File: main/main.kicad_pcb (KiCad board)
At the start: 2 copper layers, 17.8 x 43.2 mm, 6 parts, among them P1 Digital, P2 Analog, P3 CONN_01X01, P4 CONN_01X01, P5 CONN_01X01, P6 CONN_01X01

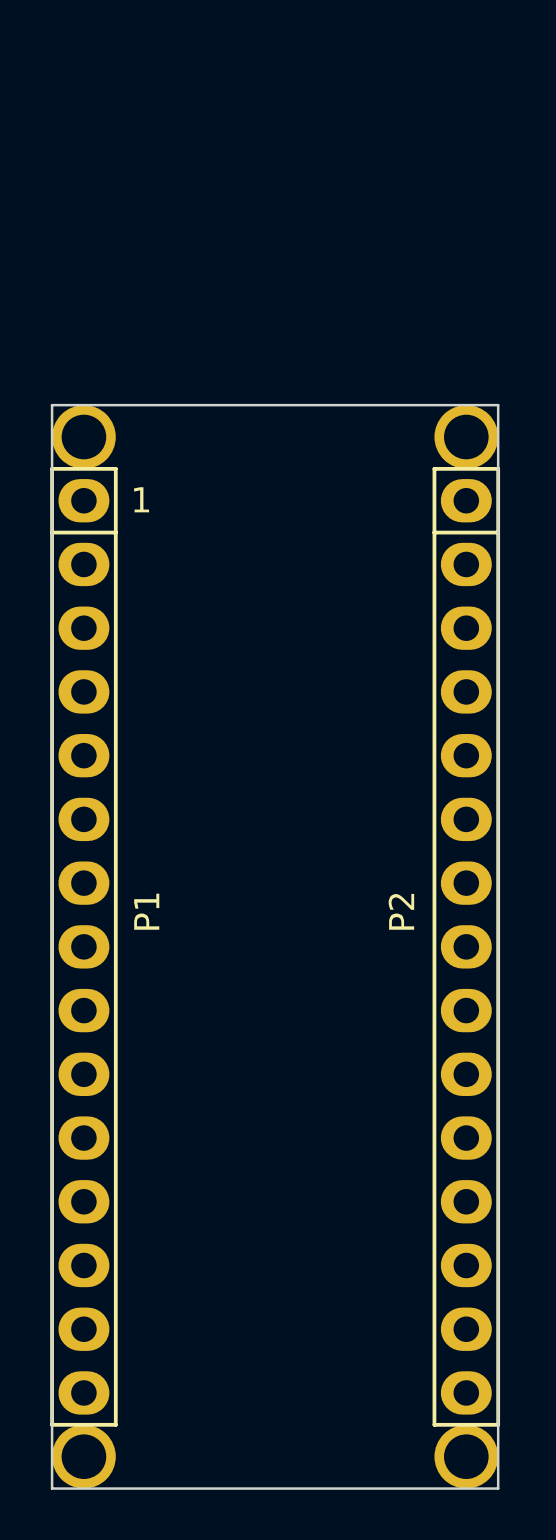
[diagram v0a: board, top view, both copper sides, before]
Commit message: main.pcb: Enlarged outline of board and translated mounting holes
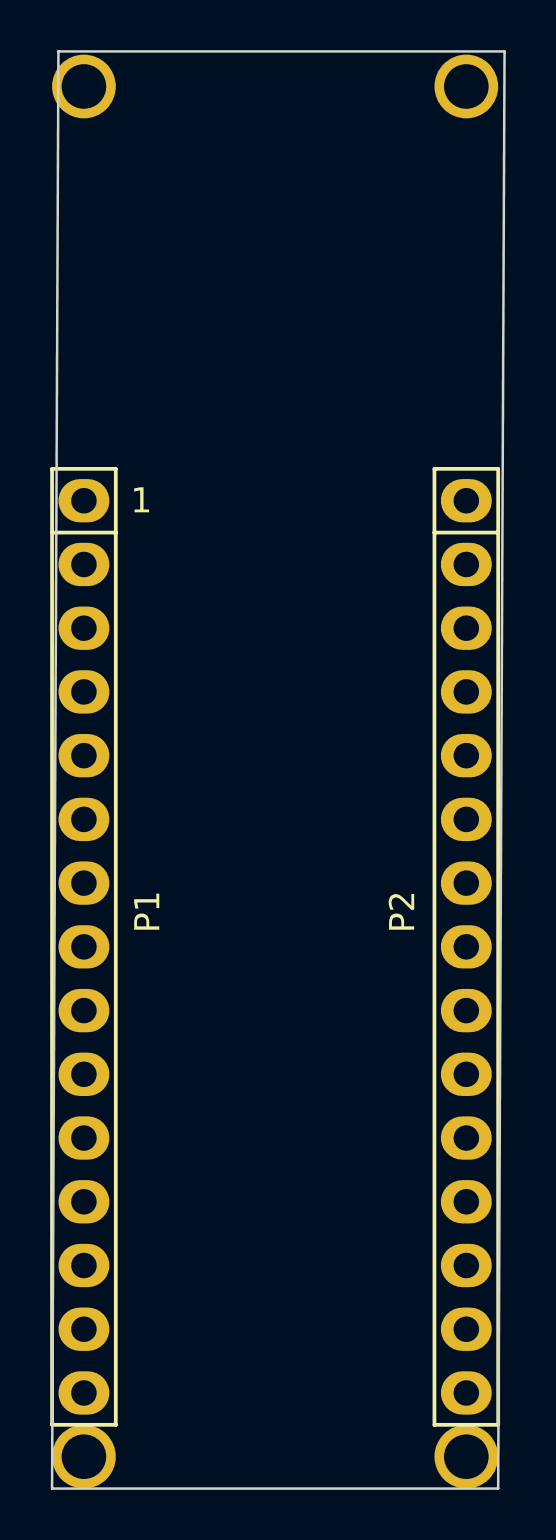
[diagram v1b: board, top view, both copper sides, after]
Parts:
- moved P3 14.0 mm to (139.4, 54.7)
- moved P6 14.0 mm to (154.7, 54.7)
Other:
- board size 17.8 x 43.2 mm -> 18 x 57.3 mm
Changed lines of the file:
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@@
   )
   (module Socket_Arduino_Nano:1pin_Nano locked (layer F.Cu)
-    (at 139.446 68.707)
+    (at 139.446 54.737)
     (descr "module 1 pin (ou trou mecanique de percage)")
     (tags DEV)
@@
   )
   (module Socket_Arduino_Nano:1pin_Nano locked (layer F.Cu)
-    (at 154.686 68.707)
+    (at 154.686 54.737)
     (descr "module 1 pin (ou trou mecanique de percage)")
     (tags DEV)
@@
   (gr_line (start 143.256 72.517) (end 150.876 72.517) (angle 90) (layer Dwgs.User) (width 0.15))
   (gr_line (start 143.256 67.437) (end 143.256 72.517) (angle 90) (layer Dwgs.User) (width 0.15))
-  (gr_line (start 138.176 67.437) (end 138.176 110.617) (angle 90) (layer Edge.Cuts) (width 0.1))
-  (gr_line (start 155.956 67.437) (end 138.176 67.437) (angle 90) (layer Edge.Cuts) (width 0.1))
-  (gr_line (start 155.956 110.617) (end 155.956 67.437) (angle 90) (layer Edge.Cuts) (width 0.1))
+  (gr_line (start 138.43 53.34) (end 138.176 110.617) (angle 90) (layer Edge.Cuts) (width 0.1))
+  (gr_line (start 156.21 53.34) (end 138.43 53.34) (angle 90) (layer Edge.Cuts) (width 0.1))
+  (gr_line (start 155.956 110.617) (end 156.21 53.34) (angle 90) (layer Edge.Cuts) (width 0.1))
   (gr_line (start 138.176 110.617) (end 155.956 110.617) (angle 90) (layer Edge.Cuts) (width 0.1))
 )

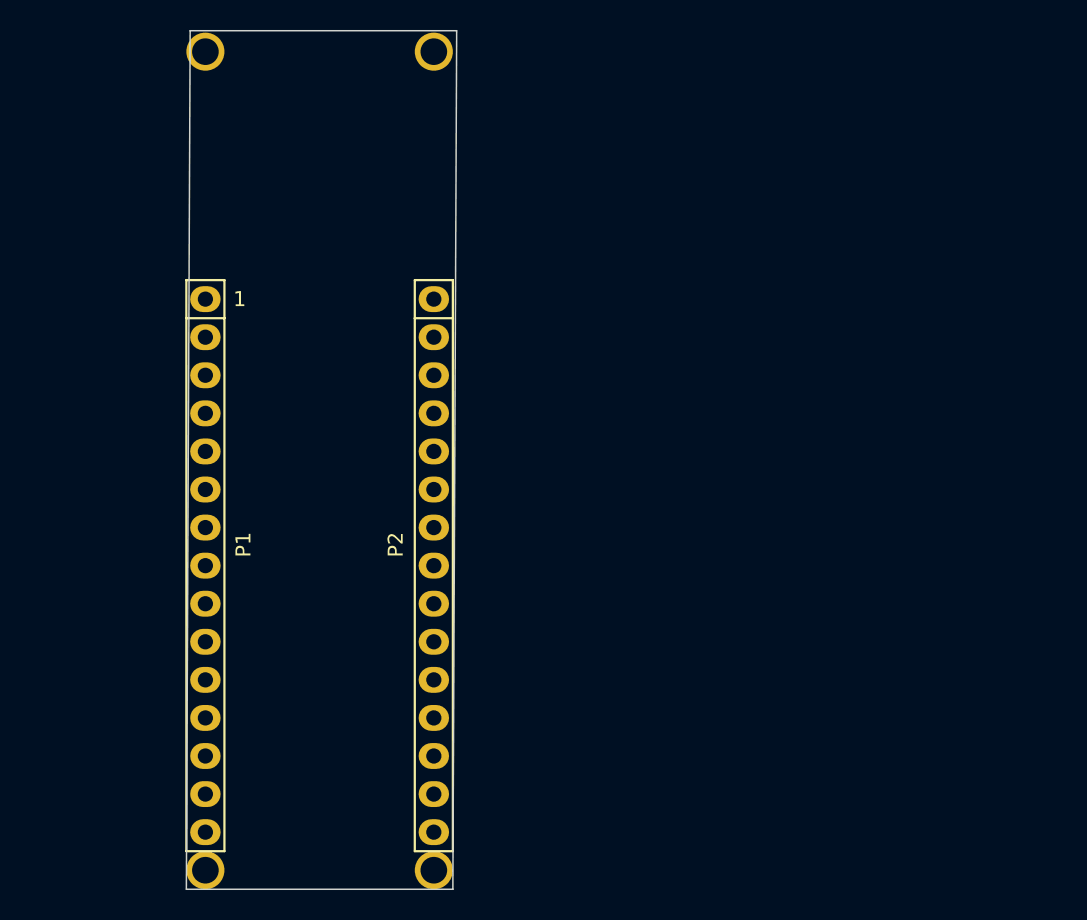
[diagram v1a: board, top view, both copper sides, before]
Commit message: pcb: Performed preliminary layout without traces
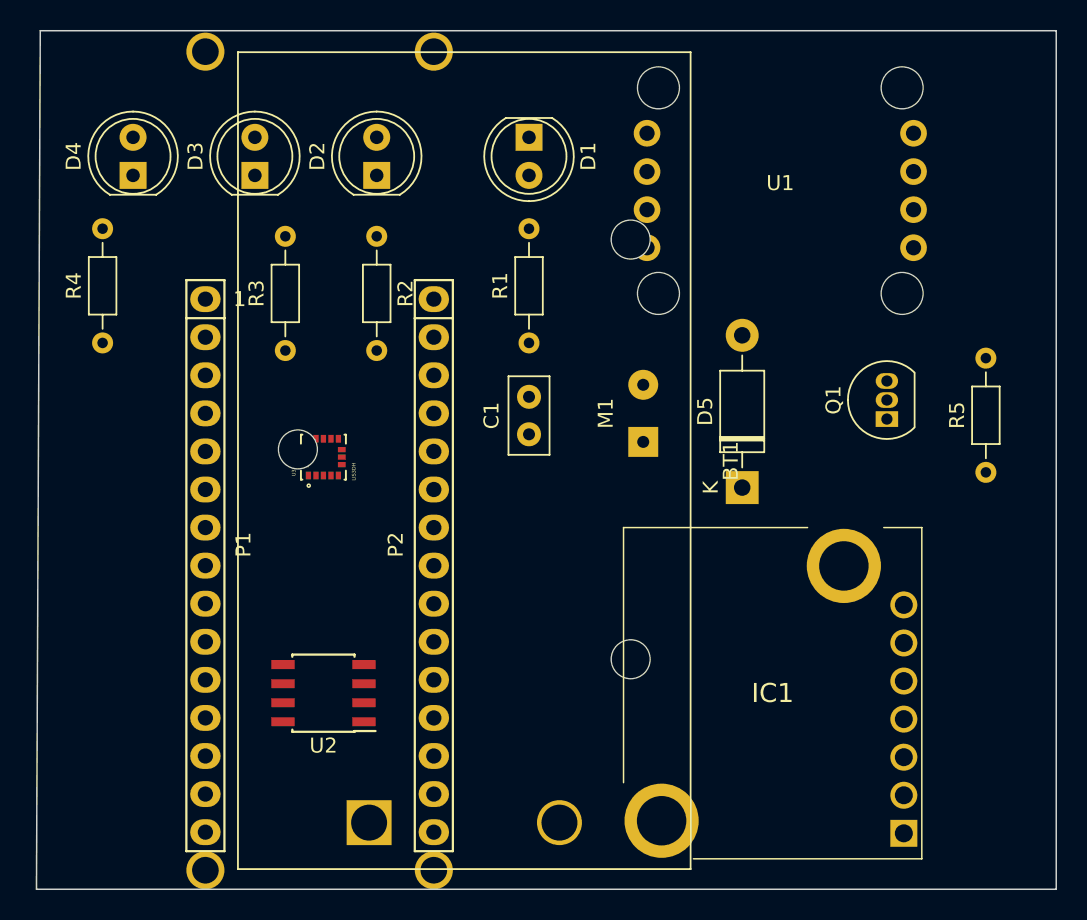
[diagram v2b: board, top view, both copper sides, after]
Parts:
- added BT1: Battery, Battery:BatteryHolder_Eagle_12BH611-GR, F.Cu at (150.4, 106.2)
- added C1: 0.1 uF, Capacitor_THT:C_Disc_D5.0mm_W2.5mm_P2.50mm, F.Cu at (161.0, 80.3)
- added D1: PWR_GREEN, LED_THT:LED_D5.0mm, F.Cu at (161.0, 60.5)
- added D2: MTR_RED, LED_THT:LED_D5.0mm, F.Cu at (150.9, 63.0)
- added D3: USONIC_BLUE, LED_THT:LED_D5.0mm, F.Cu at (142.7, 63.0)
- added D4: TEMP_YELLOW, LED_THT:LED_D5.0mm, F.Cu at (134.6, 63.0)
- added D5: 1N4001, Diode_THT:D_DO-41_SOD81_P10.16mm_Horizontal, F.Cu at (175.3, 83.8)
- added IC1: MB1010-000, MB1010-000:MB1010000, F.Cu at (177.3, 97.5)
- added M1: Motor_DC, Connector_Wire:SolderWirePad_1x02_P3.81mm_Drill0.8mm, F.Cu at (168.7, 80.8)
- added Q1: PN2222A, Package_TO_SOT_THT:TO-92_Inline, F.Cu at (184.9, 79.2)
- added R1: 1K, Resistor_THT:R_Axial_DIN0204_L3.6mm_D1.6mm_P7.62mm_Horizontal, F.Cu at (161.0, 74.2)
- added R2: 1K, Resistor_THT:R_Axial_DIN0204_L3.6mm_D1.6mm_P7.62mm_Horizontal, F.Cu at (150.9, 67.1)
- added R3: 1K, Resistor_THT:R_Axial_DIN0204_L3.6mm_D1.6mm_P7.62mm_Horizontal, F.Cu at (144.8, 74.7)
- added R4: 1K, Resistor_THT:R_Axial_DIN0204_L3.6mm_D1.6mm_P7.62mm_Horizontal, F.Cu at (132.6, 74.2)
- added R5: 1K, Resistor_THT:R_Axial_DIN0204_L3.6mm_D1.6mm_P7.62mm_Horizontal, F.Cu at (191.5, 82.8)
- added U1: SW_PWR_BTN, 1400:1400-PWR-SW, F.Cu at (177.8, 64.0)
- added U2: TMP36xS, Package_SO:SOIC-8_3.9x4.9mm_P1.27mm, F.Cu at (147.3, 97.5)
- added U3: LIS3DH, PQFN50P300X300X100-16N, F.Cu at (147.3, 81.8)
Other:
- board size 18 x 57.3 mm -> 68 x 57.3 mm

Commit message: pcb: Updated netlist with new TMP36 sensor and re-arranged layout
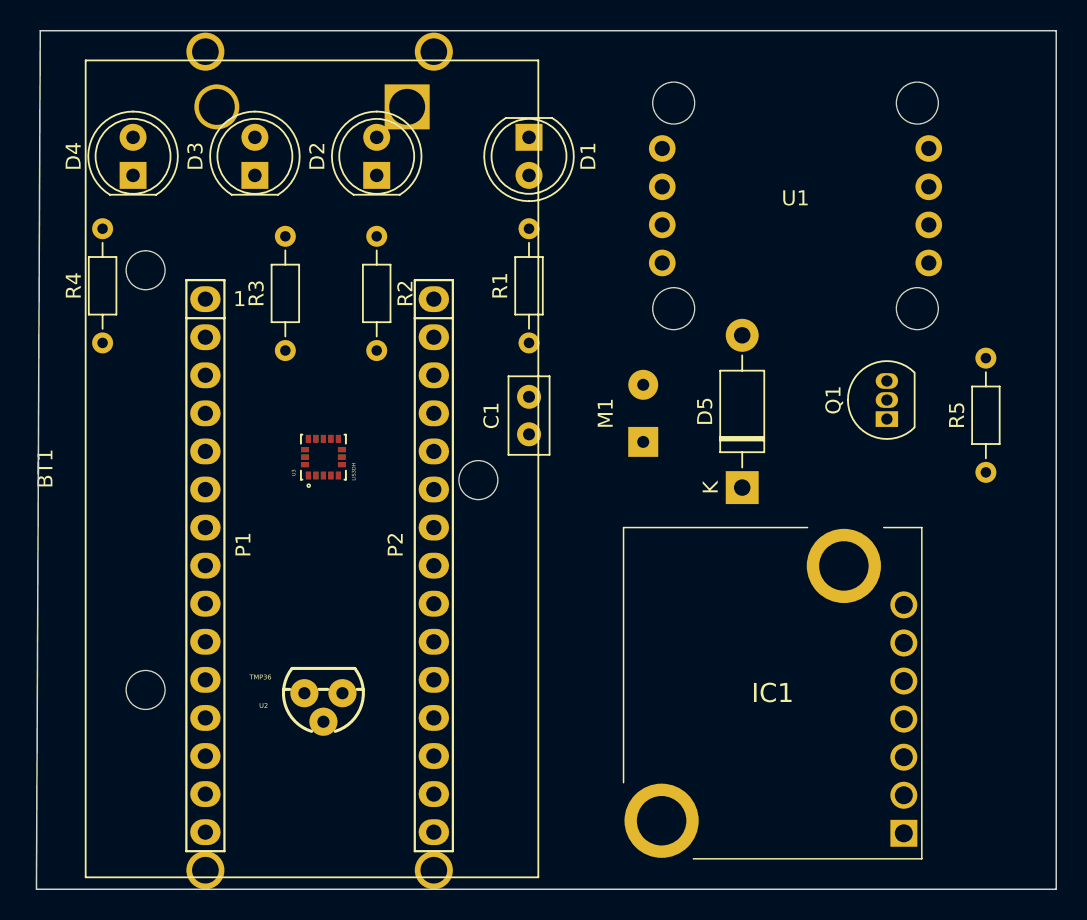
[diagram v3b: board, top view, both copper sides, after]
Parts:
- U2: value TMP36xS -> TMP36; footprint Package_SO:SOIC-8_3.9x4.9mm_P1.27mm -> TMP36:TO-92
- moved BT1 47.8 mm to (152.9, 58.4), turned to 90 degrees
- moved U1 1.44 mm to (178.8, 65.0)
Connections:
- net Net-(BT1-Pad1) renamed /Battery
- U1 pad 4: Net-(U1-Pad4) -> /A6
- U2 pad 1: /A0 -> +5V
- U2 pad 2: (no net) -> /A0
- U2 pad 3: (no net) -> GND
